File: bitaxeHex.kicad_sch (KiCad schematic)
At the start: 21 parts, among them J1 Screw Terminal, J2 Conn_01x01

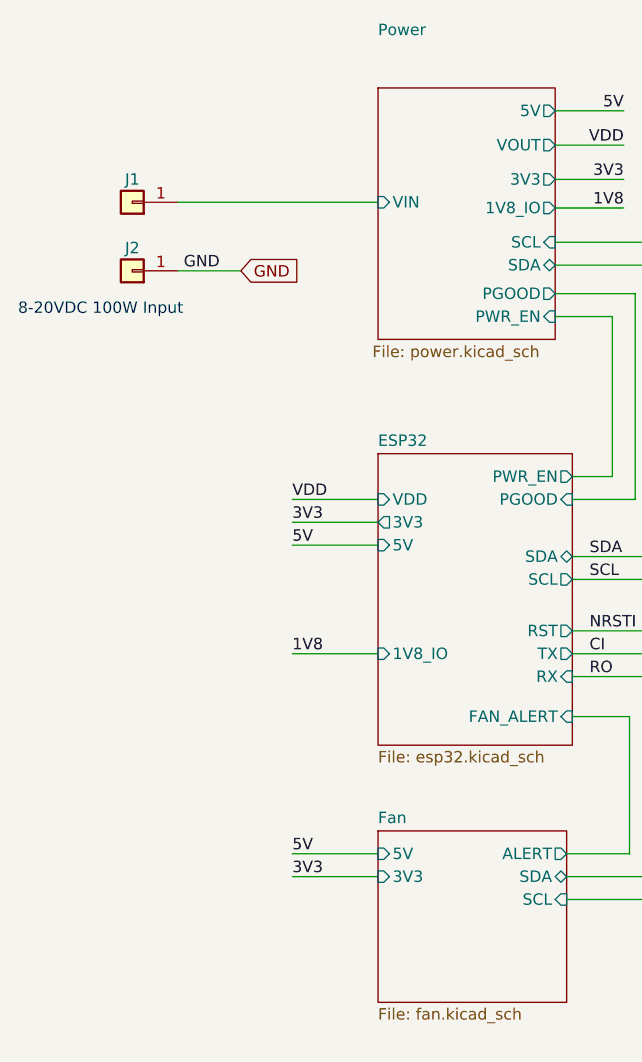
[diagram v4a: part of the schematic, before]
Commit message: remove old 5V power supply, prepare footprints for new 5V buck supply, switch fans to 12V
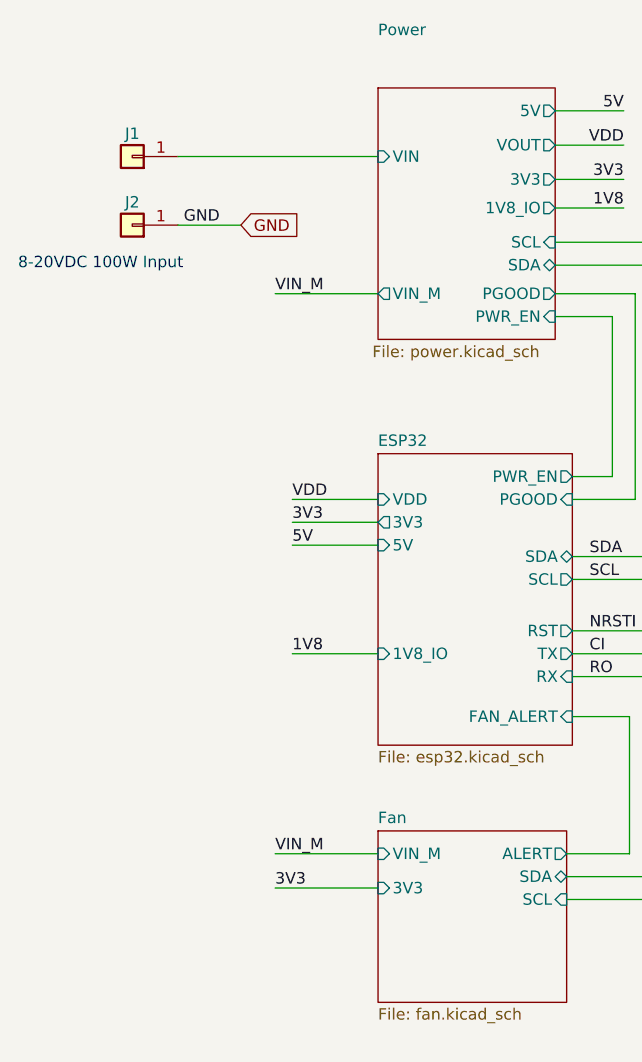
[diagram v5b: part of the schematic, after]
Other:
- sheet Fan ports: added VIN_M; removed 5V
- sheet Power ports: added VIN_M; removed none
- moved on the sheet: J1, J2
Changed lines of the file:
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@@
+    (stroke (width 0) (type default))
+  )
+  (wire (pts (xy 48.26 110.49) (xy 59.69 110.49))
     (stroke (width 0) (type default))
   )
@@
     (stroke (width 0) (type default))
   )
-  (wire (pts (xy 37.465 45.72) (xy 44.45 45.72))
+  (wire (pts (xy 37.465 40.64) (xy 44.45 40.64))
     (stroke (width 0) (type default))
   )
@@
     (stroke (width 0) (type default))
   )
-  (wire (pts (xy 50.165 113.03) (xy 59.69 113.03))
-    (stroke (width 0) (type default))
-  )
   (wire (pts (xy 93.345 45.085) (xy 79.375 45.085))
     (stroke (width 0) (type default))
@@
     (stroke (width 0) (type default))
   )
+  (wire (pts (xy 48.26 114.3) (xy 59.69 114.3))
+    (stroke (width 0) (type default))
+  )
   (wire (pts (xy 141.605 99.06) (xy 154.94 99.06))
     (stroke (width 0) (type default))
@@
     (stroke (width 0) (type default))
   )
+  (wire (pts (xy 48.26 48.26) (xy 59.69 48.26))
+    (stroke (width 0) (type default))
+  )
   (wire (pts (xy 81.28 88.265) (xy 123.825 88.265))
     (stroke (width 0) (type default))
@@
     (stroke (width 0) (type default))
   )
-  (wire (pts (xy 50.165 110.49) (xy 59.69 110.49))
-    (stroke (width 0) (type default))
-  )
   (wire (pts (xy 81.28 68.58) (xy 85.725 68.58))
     (stroke (width 0) (type default))
@@
     (stroke (width 0) (type default))
   )
-  (wire (pts (xy 37.465 38.1) (xy 59.69 38.1))
+  (wire (pts (xy 37.465 33.02) (xy 59.69 33.02))
     (stroke (width 0) (type default))
   )
@@
     (effects (font (face "Ayuthaya") (size 3 3) italic) (justify left bottom))
   )
-  (text "8-20VDC 100W Input" (at 19.685 50.8 0)
+  (text "8-20VDC 100W Input" (at 19.685 45.72 0)
+    (effects (font (size 1.27 1.27)) (justify left bottom))
+  )
+  (label "VIN_M" (at 48.26 48.26 0) (fields_autoplaced)
     (effects (font (size 1.27 1.27)) (justify left bottom))
   )
@@
     (effects (font (size 1.27 1.27)) (justify left bottom))
   )
-  (label "5V" (at 50.165 110.49 0) (fields_autoplaced)
-    (effects (font (size 1.27 1.27)) (justify left bottom))
-  )
   (label "SDA" (at 83.185 77.47 0) (fields_autoplaced)
     (effects (font (size 1.27 1.27)) (justify left bottom))
@@
     (effects (font (size 1.27 1.27)) (justify left bottom))
   )
+  (label "VIN_M" (at 48.26 110.49 0) (fields_autoplaced)
+    (effects (font (size 1.27 1.27)) (justify left bottom))
+  )
   (label "SCL" (at 83.185 80.01 0) (fields_autoplaced)
     (effects (font (size 1.27 1.27)) (justify left bottom))
@@
     (effects (font (size 1.27 1.27)) (justify left bottom))
   )
-  (label "3V3" (at 50.165 113.03 0) (fields_autoplaced)
-    (effects (font (size 1.27 1.27)) (justify left bottom))
-  )
-  (label "GND" (at 38.1 45.72 0) (fields_autoplaced)
+  (label "3V3" (at 48.26 114.3 0) (fields_autoplaced)
+    (effects (font (size 1.27 1.27)) (justify left bottom))
+  )
+  (label "GND" (at 38.1 40.64 0) (fields_autoplaced)
     (effects (font (size 1.27 1.27)) (justify left bottom))
   )
@@
     (effects (font (size 1.27 1.27)) (justify right bottom))
   )
-  (global_label "GND" (shape input) (at 44.45 45.72 0) (fields_autoplaced)
+  (global_label "GND" (shape input) (at 44.45 40.64 0) (fields_autoplaced)
     (effects (font (size 1.27 1.27)) (justify left))
-    (property "Intersheetrefs" "${INTERSHEET_REFS}" (at 50.7336 45.6406 0)
+    (property "Intersheetrefs" "${INTERSHEET_REFS}" (at 50.7336 40.5606 0)
       (effects (font (size 1.27 1.27)) (justify left) hide)
     )
   )
-  (symbol (lib_id "Connector_Generic:Conn_01x01") (at 32.385 38.1 180) (unit 1)
+  (symbol (lib_id "Connector_Generic:Conn_01x01") (at 32.385 33.02 180) (unit 1)
     (in_bom yes) (on_board yes) (dnp no)
-    (property "Reference" "J1" (at 32.385 35.56 0)
+    (property "Reference" "J1" (at 32.385 30.48 0)
       (effects (font (size 1.27 1.27)))
     )
-    (property "Value" "Screw Terminal" (at 32.385 34.29 0)
-      (effects (font (size 1.27 1.27)) hide)
-    )
-    (property "Footprint" "bitaxe:7770-screw-terminal" (at 32.385 38.1 0)
-      (effects (font (size 1.27 1.27)) hide)
-    )
-    (property "Datasheet" "https://mm.digikey.com/Volume0/opasdata/d220001/medias/docus/581/Metric_PCB_Screw_Terminals.pdf" (at 32.385 38.1 0)
-      (effects (font (size 1.27 1.27)) hide)
-    )
-    (property "DK" "36-7770-ND" (at 32.385 38.1 0)
-      (effects (font (size 1.27 1.27)) hide)
-    )
-    (property "PARTNO" "36-7770" (at 32.385 38.1 0)
+    (property "Value" "Screw Terminal" (at 32.385 29.21 0)
+      (effects (font (size 1.27 1.27)) hide)
+    )
+    (property "Footprint" "bitaxe:7770-screw-terminal" (at 32.385 33.02 0)
+      (effects (font (size 1.27 1.27)) hide)
+    )
+    (property "Datasheet" "https://mm.digikey.com/Volume0/opasdata/d220001/medias/docus/581/Metric_PCB_Screw_Terminals.pdf" (at 32.385 33.02 0)
+      (effects (font (size 1.27 1.27)) hide)
+    )
+    (property "DK" "36-7770-ND" (at 32.385 33.02 0)
+      (effects (font (size 1.27 1.27)) hide)
+    )
+    (property "PARTNO" "36-7770" (at 32.385 33.02 0)
       (effects (font (size 1.27 1.27)) hide)
     )
@@
     )
   )
-  (symbol (lib_id "Connector_Generic:Conn_01x01") (at 32.385 45.72 180) (unit 1)
+  (symbol (lib_id "Connector_Generic:Conn_01x01") (at 32.385 40.64 180) (unit 1)
     (in_bom yes) (on_board yes) (dnp no)
-    (property "Reference" "J2" (at 32.385 43.18 0)
+    (property "Reference" "J2" (at 32.385 38.1 0)
       (effects (font (size 1.27 1.27)))
     )
-    (property "Value" "Conn_01x01" (at 32.385 41.91 0)
-      (effects (font (size 1.27 1.27)) hide)
-    )
-    (property "Footprint" "bitaxe:7770-screw-terminal" (at 32.385 45.72 0)
-      (effects (font (size 1.27 1.27)) hide)
-    )
-    (property "Datasheet" "https://www.te.com/commerce/DocumentDelivery/DDEController?Action=srchrtrv&DocNm=63862&DocType=Customer+Drawing&DocLang=English" (at 32.385 45.72 0)
-      (effects (font (size 1.27 1.27)) hide)
-    )
-    (property "DK" "A100886CT-ND" (at 32.385 45.72 0)
-      (effects (font (size 1.27 1.27)) hide)
-    )
-    (property "PARTNO" "63862-1" (at 32.385 45.72 0)
+    (property "Value" "Conn_01x01" (at 32.385 36.83 0)
+      (effects (font (size 1.27 1.27)) hide)
+    )
+    (property "Footprint" "bitaxe:7770-screw-terminal" (at 32.385 40.64 0)
+      (effects (font (size 1.27 1.27)) hide)
+    )
+    (property "Datasheet" "https://www.te.com/commerce/DocumentDelivery/DDEController?Action=srchrtrv&DocNm=63862&DocType=Customer+Drawing&DocLang=English" (at 32.385 40.64 0)
+      (effects (font (size 1.27 1.27)) hide)
+    )
+    (property "DK" "A100886CT-ND" (at 32.385 40.64 0)
+      (effects (font (size 1.27 1.27)) hide)
+    )
+    (property "PARTNO" "63862-1" (at 32.385 40.64 0)
       (effects (font (size 1.27 1.27)) hide)
     )
@@
       (effects (font (size 1.27 1.27)) (justify right))
     )
-    (pin "5V" input (at 59.69 110.49 180)
-      (effects (font (size 1.27 1.27)) (justify left))
-    )
-    (pin "3V3" input (at 59.69 113.03 180)
+    (pin "3V3" input (at 59.69 114.3 180)
       (effects (font (size 1.27 1.27)) (justify left))
     )
     (pin "ALERT" output (at 80.645 110.49 0)
       (effects (font (size 1.27 1.27)) (justify right))
+    )
+    (pin "VIN_M" input (at 59.69 110.49 180)
+      (effects (font (size 1.27 1.27)) (justify left))
     )
     (instances
@@
       (effects (font (size 1.27 1.27)) (justify right))
     )
-    (pin "VIN" input (at 59.69 38.1 180)
+    (pin "VIN" input (at 59.69 33.02 180)
       (effects (font (size 1.27 1.27)) (justify left))
     )
@@
       (effects (font (size 1.27 1.27)) (justify right))
     )
-    (instances
+    (pin "VIN_M" output (at 59.69 48.26 180)
+      (effects (font (size 1.27 1.27)) (justify left))
+    )
+    (instances

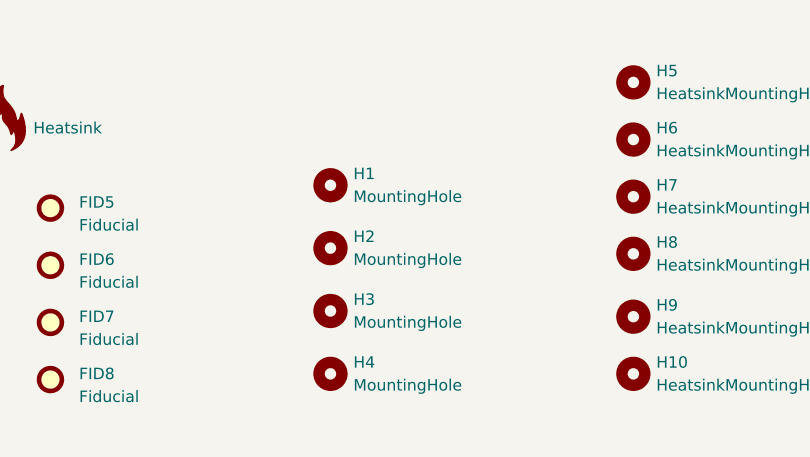
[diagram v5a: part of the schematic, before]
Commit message: fix warnings on H3 and H4 mounting holes
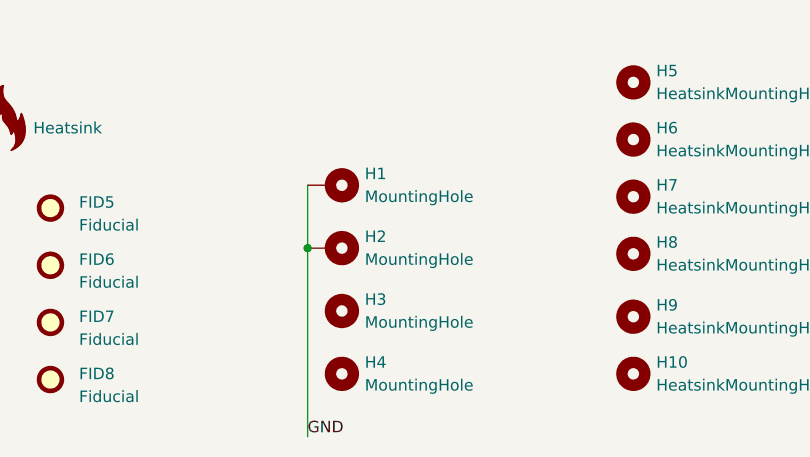
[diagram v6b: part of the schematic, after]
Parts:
- H1, H2: symbol Mechanical:MountingHole -> Mechanical:MountingHole_Pad; now in the parts list
- H3, H4: footprint MountingHole:MountingHole_3mm_Pad_Via -> MountingHole:MountingHole_3mm; now in the parts list
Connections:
- net GND: now also H1.1, H2.1
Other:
- moved on the sheet: H3, H4
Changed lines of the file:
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@@
   (junction (at 120.015 114.935) (diameter 0) (color 0 0 0 0)
   )
+  (junction (at 82.55 176.53) (diameter 0) (color 0 0 0 0)
+  )
   (junction (at 93.345 77.47) (diameter 0) (color 0 0 0 0)
   )
@@
   )
   (wire (pts (xy 123.825 85.725) (xy 81.28 85.725))
+    (stroke (width 0) (type default))
+  )
+  (wire (pts (xy 82.55 176.53) (xy 82.55 197.485))
+    (stroke (width 0) (type default))
+  )
+  (wire (pts (xy 82.55 169.545) (xy 82.55 176.53))
     (stroke (width 0) (type default))
   )
@@
   )
   (label "NRSTI" (at 83.185 85.725 0) (fields_autoplaced)
+    (effects (font (size 1.27 1.27)) (justify left bottom))
+  )
+  (label "GND" (at 82.55 197.485 0) (fields_autoplaced)
     (effects (font (size 1.27 1.27)) (justify left bottom))
   )
@@
     )
   )
-  (symbol (lib_id "Mechanical:MountingHole") (at 85.09 190.5 0) (unit 1)
-    (in_bom no) (on_board yes) (dnp no) (fields_autoplaced)
-    (property "Reference" "H4" (at 87.63 189.2299 0)
-      (effects (font (size 1.27 1.27)) (justify left))
-    )
-    (property "Value" "MountingHole" (at 87.63 191.7699 0)
-      (effects (font (size 1.27 1.27)) (justify left))
-    )
-    (property "Footprint" "MountingHole:MountingHole_3mm_Pad_Via" (at 85.09 190.5 0)
-      (effects (font (size 1.27 1.27)) hide)
-    )
-    (property "Datasheet" "~" (at 85.09 190.5 0)
+  (symbol (lib_id "Mechanical:MountingHole") (at 86.36 190.5 270) (unit 1)
+    (in_bom yes) (on_board yes) (dnp no) (fields_autoplaced)
+    (property "Reference" "H4" (at 88.9 189.23 90)
+      (effects (font (size 1.27 1.27)) (justify left))
+    )
+    (property "Value" "MountingHole" (at 88.9 191.77 90)
+      (effects (font (size 1.27 1.27)) (justify left))
+    )
+    (property "Footprint" "MountingHole:MountingHole_3mm" (at 86.36 190.5 0)
+      (effects (font (size 1.27 1.27)) hide)
+    )
+    (property "Datasheet" "~" (at 86.36 190.5 0)
       (effects (font (size 1.27 1.27)) hide)
     )
@@
     )
   )
-  (symbol (lib_id "Mechanical:MountingHole") (at 85.09 169.545 0) (unit 1)
-    (in_bom no) (on_board yes) (dnp no) (fields_autoplaced)
-    (property "Reference" "H1" (at 87.63 168.2749 0)
-      (effects (font (size 1.27 1.27)) (justify left))
-    )
-    (property "Value" "MountingHole" (at 87.63 170.8149 0)
+  (symbol (lib_id "Mechanical:MountingHole_Pad") (at 85.09 169.545 270) (unit 1)
+    (in_bom yes) (on_board yes) (dnp no) (fields_autoplaced)
+    (property "Reference" "H1" (at 88.9 168.275 90)
+      (effects (font (size 1.27 1.27)) (justify left))
+    )
+    (property "Value" "MountingHole" (at 88.9 170.815 90)
       (effects (font (size 1.27 1.27)) (justify left))
     )
@@
       (effects (font (size 1.27 1.27)) hide)
     )
+    (pin "1")
     (instances
       (project "bitaxeHex"
@@
     )
   )
-  (symbol (lib_id "Mechanical:MountingHole") (at 85.09 176.53 0) (unit 1)
-    (in_bom no) (on_board yes) (dnp no) (fields_autoplaced)
-    (property "Reference" "H2" (at 87.63 175.2599 0)
-      (effects (font (size 1.27 1.27)) (justify left))
-    )
-    (property "Value" "MountingHole" (at 87.63 177.7999 0)
+  (symbol (lib_id "Mechanical:MountingHole_Pad") (at 85.09 176.53 270) (unit 1)
+    (in_bom yes) (on_board yes) (dnp no) (fields_autoplaced)
+    (property "Reference" "H2" (at 88.9 175.26 90)
+      (effects (font (size 1.27 1.27)) (justify left))
+    )
+    (property "Value" "MountingHole" (at 88.9 177.8 90)
       (effects (font (size 1.27 1.27)) (justify left))
     )
@@
       (effects (font (size 1.27 1.27)) hide)
     )
+    (pin "1")
     (instances
       (project "bitaxeHex"
@@
     )
   )
-  (symbol (lib_id "Mechanical:MountingHole") (at 85.09 183.515 0) (unit 1)
-    (in_bom no) (on_board yes) (dnp no) (fields_autoplaced)
-    (property "Reference" "H3" (at 87.63 182.2449 0)
-      (effects (font (size 1.27 1.27)) (justify left))
-    )
-    (property "Value" "MountingHole" (at 87.63 184.7849 0)
-      (effects (font (size 1.27 1.27)) (justify left))
-    )
-    (property "Footprint" "MountingHole:MountingHole_3mm_Pad_Via" (at 85.09 183.515 0)
-      (effects (font (size 1.27 1.27)) hide)
-    )
-    (property "Datasheet" "~" (at 85.09 183.515 0)
-      (effects (font (size 1.27 1.27)) hide)
-    )
+  (symbol (lib_id "Mechanical:MountingHole") (at 86.36 183.515 270) (unit 1)
+    (in_bom yes) (on_board yes) (dnp no) (fields_autoplaced)
+    (property "Reference" "H3" (at 88.9 182.245 90)
+      (effects (font (size 1.27 1.27)) (justify left))
+    )
+    (property "Value" "MountingHole" (at 88.9 184.785 90)
+      (effects (font (size 1.27 1.27)) (justify left))
+    )
+    (property "Footprint" "MountingHole:MountingHole_3mm" (at 86.36 183.515 0)
+      (effects (font (size 1.27 1.27)) hide)
+    )
+    (property "Datasheet" "~" (at 86.36 183.515 0)
+      (effects (font (size 1.27 1.27)) hide)
+    )

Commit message: small schematic cleanup
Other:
- note added: "12VDC 100W Input"
- note removed: "8-20VDC 100W Input"
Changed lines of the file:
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@@
     (effects (font (face "Ayuthaya") (size 3 3) italic) (justify left bottom))
   )
-  (text "8-20VDC 100W Input" (at 19.685 45.72 0)
+  (text "12VDC 100W Input" (at 19.685 45.72 0)
     (effects (font (size 1.27 1.27)) (justify left bottom))
   )
@@
     (stroke (width 0.1524) (type solid))
     (fill (color 255 255 194 1.0000))
-    (property "Sheetname" "Power" (at 59.69 19.685 0)
+    (property "Sheetname" "Power" (at 59.69 24.765 0)
       (effects (font (size 1.27 1.27)) (justify left bottom))
     )

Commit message: screw terminal partno update
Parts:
- J2: value Conn_01x01 -> Screw Terminal; DK A100886CT-ND -> 36-7770-ND; PARTNO 63862-1 -> 36-7770
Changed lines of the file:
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@@
       (effects (font (size 1.27 1.27)))
     )
-    (property "Value" "Conn_01x01" (at 32.385 36.83 0)
+    (property "Value" "Screw Terminal" (at 32.385 36.83 0)
       (effects (font (size 1.27 1.27)) hide)
     )
@@
       (effects (font (size 1.27 1.27)) hide)
     )
-    (property "DK" "A100886CT-ND" (at 32.385 40.64 0)
+    (property "DK" "36-7770-ND" (at 32.385 40.64 0)
       (effects (font (size 1.27 1.27)) hide)
     )
-    (property "PARTNO" "63862-1" (at 32.385 40.64 0)
+    (property "PARTNO" "36-7770" (at 32.385 40.64 0)
       (effects (font (size 1.27 1.27)) hide)
     )
